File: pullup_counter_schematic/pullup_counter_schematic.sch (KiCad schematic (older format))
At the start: 53 parts, among them J1 FOUR_WIRE_CONN, J2 READ_PORT, Q1 MMBT3904, Q2 MMBT3904, Q3 MMBT3904, Q4 MMBT3906, SW1 SW_Push, U1 LM358, U2 HT7333, U3 P25Q40H, U4 dual_sev_seg_display, U5 AT24C02, U6 STM32F031C6Tx, Y1 32.768KHz

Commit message: Uploaded offline work
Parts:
- removed BT1: Battery, Connector_PinHeader_2.54mm:PinHeader_1x02_P2.54mm_Vertical, symbol Device:Battery
- removed C1, C6: 1uF, Capacitor_SMD:C_1206_3216Metric_Pad1.33x1.80mm_HandSolder, symbol Device:C
- removed J1: FOUR_WIRE_CONN, Connector_PinHeader_2.54mm:PinHeader_1x04_P2.54mm_Vertical, symbol MYCLEO:FOUR_WIRE_CONN
- removed J2: READ_PORT, Connector_PinSocket_2.54mm:PinSocket_2x03_P2.54mm_Vertical, symbol Connector:Conn_01x06_Male
- removed JP1: Jumper_2_Open, Jumper:SolderJumper-2_P1.3mm_Open_RoundedPad1.0x1.5mm, symbol Jumper:Jumper_2_Open
- removed JP2: Jumper_3_Open, Connector_PinSocket_2.54mm:PinSocket_1x03_P2.54mm_Vertical, symbol Jumper:Jumper_3_Open
- removed R1: 10K, Resistor_SMD:R_0805_2012Metric_Pad1.20x1.40mm_HandSolder, symbol Device:R
- removed R13, R14: R, Resistor_SMD:R_0805_2012Metric_Pad1.20x1.40mm_HandSolder, symbol Device:R
- removed R2: R_PHOTO, OptoDevice:R_LDR_5.0x4.1mm_P3mm_Vertical, symbol Device:R_PHOTO
- removed RN1: Voltage_Divider, Potentiometer_THT:Potentiometer_Piher_PT-10-V05_Vertical, symbol Device:Voltage_Divider
- removed U1: LM358, Package_SO:SOIC-8_3.9x4.9mm_P1.27mm, symbol Amplifier_Operational:LM358
- removed U5: AT24C02, Package_SO:SOIC-8_3.9x4.9mm_P1.27mm, symbol Memory_EEPROM:AT24CS02-SSHM
- removed U6: STM32F031C6Tx, Package_QFP:LQFP-48_7x7mm_P0.5mm, symbol MCU_ST_STM32F0:STM32F031C6Tx
- added BT? (x2): LR03, symbol Device:Battery_Cell
- added C? (x2): 100nF, symbol Device:C
- added C?: 10uF, symbol Device:C
- added J?: 6PinDebugPort, Connector_IDC:IDC-Header_2x03_P2.54mm_Vertical, symbol MYCLEO:6PinDebugPort
- added J?: USB_B_Micro, symbol Connector:USB_B_Micro
- added R? (x2): 220R, symbol Device:R_Small
- added R? (x2): 47K, symbol Device:R
- added R?: 47K, Resistor_SMD:R_0805_2012Metric_Pad1.20x1.40mm_HandSolder, symbol Device:R
- added SW?: boot, custom_buttons_switches:TSB008, symbol Switch:SW_Push
- added U?: CH340C, Package_SO:SOIC-16_3.9x9.9mm_P1.27mm, symbol Interface_USB:CH340C
- added U?: STM32L051C8Tx, Package_QFP:LQFP-48_7x7mm_P0.5mm, symbol MCU_ST_STM32L0:STM32L051C8Tx
- BT2: value Battery_Cell -> CR2032
- SW1: value SW_Push -> rst
- U2: value HT7333 -> HT7325
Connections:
- net labels added: +5V, MCU_RX, MCU_TX, USB_DM, USB_DP, USB_FLAG, VCC
- net labels removed: DIST_OUTA, DIST_REF, READ_PWR, ~HOLD, ~WP
- wire segments 211 -> 194
- no-connect marks 2 -> 8
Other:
- note added: "Change to 2.3V"
- note removed: "3S AA battery"
- note removed: "Comparator with hysteresis"
- moved on the sheet: BT2, C10, C11, C12, C2, C3, C4, C5, C7, C8, C9, H1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

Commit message: Created PCB
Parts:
- removed C12: 100nF, Capacitor_SMD:C_1206_3216Metric_Pad1.33x1.80mm_HandSolder, symbol Device:C
- added C10: ?pF, Capacitor_SMD:C_0805_2012Metric_Pad1.18x1.45mm_HandSolder, symbol Device:C
- added C14, C9: 100nF, Capacitor_SMD:C_0805_2012Metric_Pad1.18x1.45mm_HandSolder, symbol Device:C
- added C16: 1uF, Capacitor_SMD:C_0805_2012Metric_Pad1.18x1.45mm_HandSolder, symbol Device:C
- added C7, C8: 10uF, Capacitor_SMD:C_0805_2012Metric_Pad1.18x1.45mm_HandSolder, symbol Device:C
- added D1: D_Schottky, Diode_SMD:D_SMA_Handsoldering, symbol Device:D_Schottky
- added Q5: MMBT3906, Package_TO_SOT_SMD:SOT-23_Handsoldering, symbol Transistor_BJT:MMBT3906
- added R13: 10K, Resistor_SMD:R_0805_2012Metric_Pad1.20x1.40mm_HandSolder, symbol Device:R
- added R21, R22, R23: R, Resistor_SMD:R_0805_2012Metric_Pad1.20x1.40mm_HandSolder, symbol Device:R
- added SW3: start, custom_buttons_switches:TSB008, symbol Switch:SW_Push
- added SW4: TouchPad, TouchPad:TouchPad_100x100, symbol TouchPad:TouchPad
- added U4: HT7325, Package_TO_SOT_SMD:SOT-89-3, symbol Regulator_Linear:HT75xx-1-SOT89
- added U6: TTP223, Package_TO_SOT_SMD:TSOT-23-6, symbol TTP:TTP223
- added U8: KTIR0711S, pullup_counter_schematic:KTIR0711S, symbol Transoptors_custom:KTIR0711S
- BT1, BT2: renamed from BT?; footprint (none) -> Battery_Custom:SMD_SMT_AAA_LR03
- C1, C2, C4: renamed from C?; footprint (none) -> Capacitor_SMD:C_0805_2012Metric_Pad1.18x1.45mm_HandSolder
- C11: renamed from C5; footprint Capacitor_SMD:C_1206_3216Metric_Pad1.33x1.80mm_HandSolder -> Capacitor_SMD:C_0805_2012Metric_Pad1.18x1.45mm_HandSolder
- C12: renamed from C7; footprint Capacitor_SMD:C_1206_3216Metric_Pad1.33x1.80mm_HandSolder -> Capacitor_SMD:C_0805_2012Metric_Pad1.18x1.45mm_HandSolder
- C13: renamed from C8; footprint Capacitor_SMD:C_1206_3216Metric_Pad1.33x1.80mm_HandSolder -> Capacitor_SMD:C_0805_2012Metric_Pad1.18x1.45mm_HandSolder
- C15: renamed from C9; footprint Capacitor_SMD:C_1206_3216Metric_Pad1.33x1.80mm_HandSolder -> Capacitor_SMD:C_0805_2012Metric_Pad1.18x1.45mm_HandSolder
- C3: renamed from C2; footprint Capacitor_SMD:C_1206_3216Metric_Pad1.33x1.80mm_HandSolder -> Capacitor_SMD:C_0805_2012Metric_Pad1.18x1.45mm_HandSolder
- C5: renamed from C3; footprint Capacitor_SMD:C_1206_3216Metric_Pad1.33x1.80mm_HandSolder -> Capacitor_SMD:C_0805_2012Metric_Pad1.18x1.45mm_HandSolder
- C6: renamed from C4; footprint Capacitor_SMD:C_1206_3216Metric_Pad1.33x1.80mm_HandSolder -> Capacitor_SMD:C_0805_2012Metric_Pad1.18x1.45mm_HandSolder
- J1: renamed from J?; footprint (none) -> Connector_USB:USB_Micro-B_Amphenol_10118194_Horizontal
- Q1, Q2, Q3, Q4: footprint Package_TO_SOT_SMD:SOT-23 -> Package_TO_SOT_SMD:SOT-23_Handsoldering
- R15, R16, R8, R9: renamed from R?; footprint (none) -> Resistor_SMD:R_0805_2012Metric_Pad1.20x1.40mm_HandSolder
- U1: renamed from U4; value dual_sev_seg_display -> COM_C
- gave numbers to parts that had none: 5
- renumbered BT2 to BT3, C10 to C17, C11 to C18, R3 to R1, R18 to R12, R12 to R14, R15 to R17, R16 to R19, R4 to R2, R17 to R20, R5 to R3, R6 to R4, R7 to R5, R8 to R6, R9 to R7, SW1 to SW2, U3 to U5
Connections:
- net labels added: DISTANCE, DISTANCE_EN, Start, TouchPin, V_BACKUP, V_MCU
- net labels removed: +3V3, DIST_OUTD, SCL, SDA
- wire segments 194 -> 273
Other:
- note added: "ADC{\nBAT_SENSE;\nDISTANCE;\n}"
- note added: "EXTI{\nStart - 7;\nTouchPin - 8;\n}"
- note added: "Start button \nin case \ntouchpad \ndoesn't work"
- note added: "TODO: ADD distance sensor\n"
- moved on the sheet: C11, C12, C13, C15, C17, C18, H1, H2, Q1, Q2, Q3, Q4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

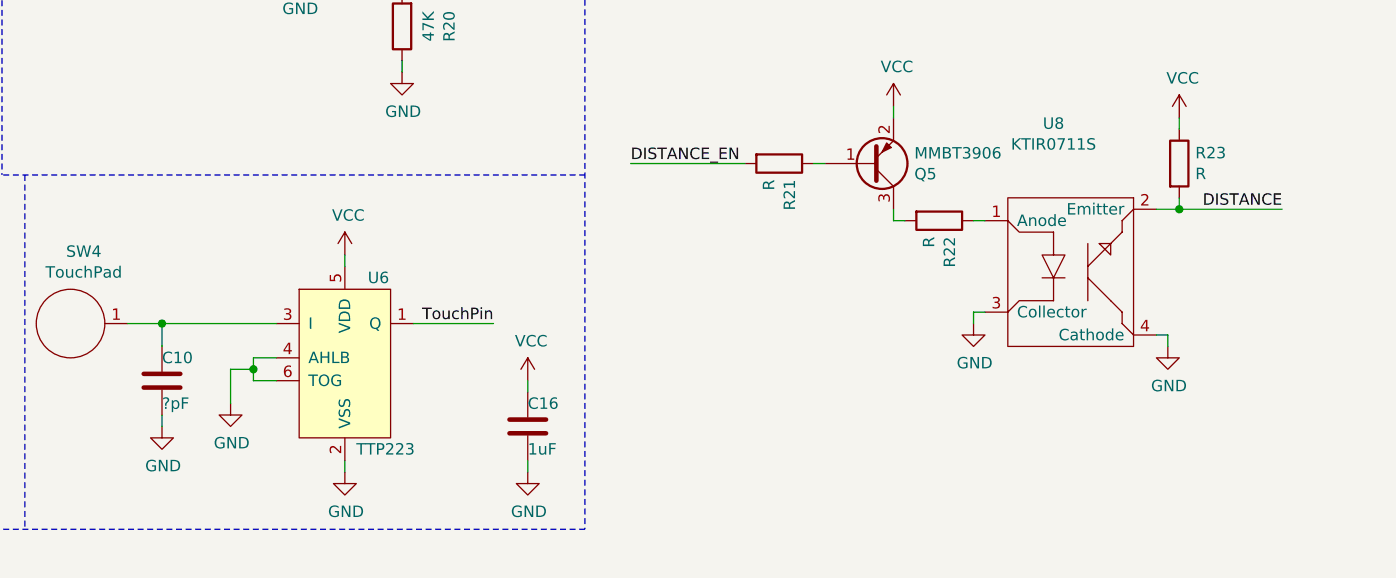
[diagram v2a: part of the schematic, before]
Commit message: Calculated value of remaining components
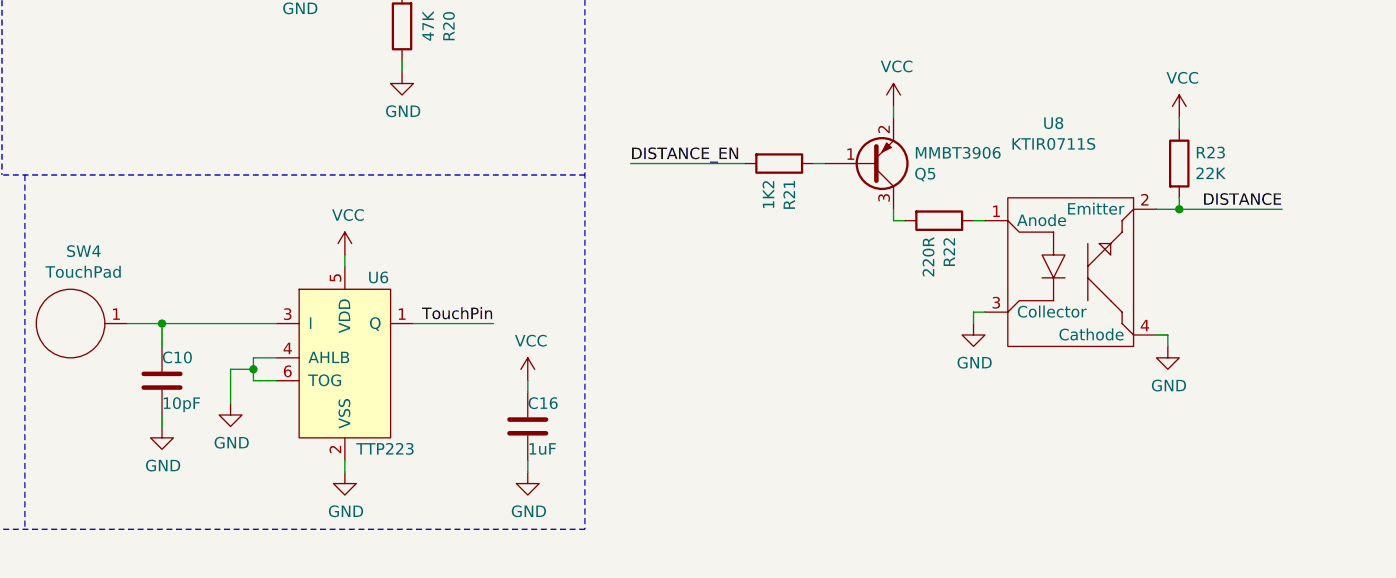
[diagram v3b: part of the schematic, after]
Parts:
- C10: value ?pF -> 10pF
- R21: value R -> 1K2
- R22: value R -> 220R
- R23: value R -> 22K
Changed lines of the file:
@@
 P 5100 6450
 F 0 "C10" H 5100 6550 50  0000 L CNN
-F 1 "?pF" H 5100 6350 50  0000 L CNN
+F 1 "10pF" H 5100 6350 50  0000 L CNN
 F 2 "Capacitor_SMD:C_0805_2012Metric_Pad1.18x1.45mm_HandSolder" H 5138 6300 50  0001 C CNN
 F 3 "~" H 5100 6450 50  0001 C CNN
@@
 P 9550 5500
 F 0 "R23" H 9620 5546 50  0000 L CNN
-F 1 "R" H 9620 5455 50  0000 L CNN
+F 1 "22K" H 9620 5455 50  0000 L CNN
 F 2 "Resistor_SMD:R_0805_2012Metric_Pad1.20x1.40mm_HandSolder" V 9480 5500 50  0001 C CNN
 F 3 "~" H 9550 5500 50  0001 C CNN
@@
 P 8500 5750
 F 0 "R22" H 8570 5796 50  0000 L CNN
-F 1 "R" H 8570 5705 50  0000 L CNN
+F 1 "220R" H 8570 5705 50  0000 L CNN
 F 2 "Resistor_SMD:R_0805_2012Metric_Pad1.20x1.40mm_HandSolder" V 8430 5750 50  0001 C CNN
 F 3 "~" H 8500 5750 50  0001 C CNN
@@
 P 7800 5500
 F 0 "R21" H 7870 5546 50  0000 L CNN
-F 1 "R" H 7870 5455 50  0000 L CNN
+F 1 "1K2" H 7870 5455 50  0000 L CNN
 F 2 "Resistor_SMD:R_0805_2012Metric_Pad1.20x1.40mm_HandSolder" V 7730 5500 50  0001 C CNN
 F 3 "~" H 7800 5500 50  0001 C CNN

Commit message: Started writing readme
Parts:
- U2, U4: value HT7325 -> HT7323
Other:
- note added: "Backup Power Supply"
- note added: "Battery Level Measurement Circuit"
- note added: "Battery connectors"
- note added: "Buttons"
- note added: "Capacitive Touch Pad"
- note added: "Display"
- note added: "External Flash Memory"
- note added: "MCU"
- note added: "Main Power Supply"
- note added: "Mounting Holes"
- note added: "Programming/Debug Port"
- note added: "Proximity Sensor"
- note added: "USB User Interface"
- note removed: "ADC{\nBAT_SENSE;\nDISTANCE;\n}"
- note removed: "Change to 2.3V"
- note removed: "EXTI{\nStart - 7;\nTouchPin - 8;\n}"
- note removed: "TODO: ADD distance sensor\n"
- moved on the sheet: C12, C13, C14, C15, Q5, R21, R22, R23, U5, U8
